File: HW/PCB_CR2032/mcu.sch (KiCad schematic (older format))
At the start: 15 parts, among them U1 STM32L071CBTx, Y1 32768 Hz

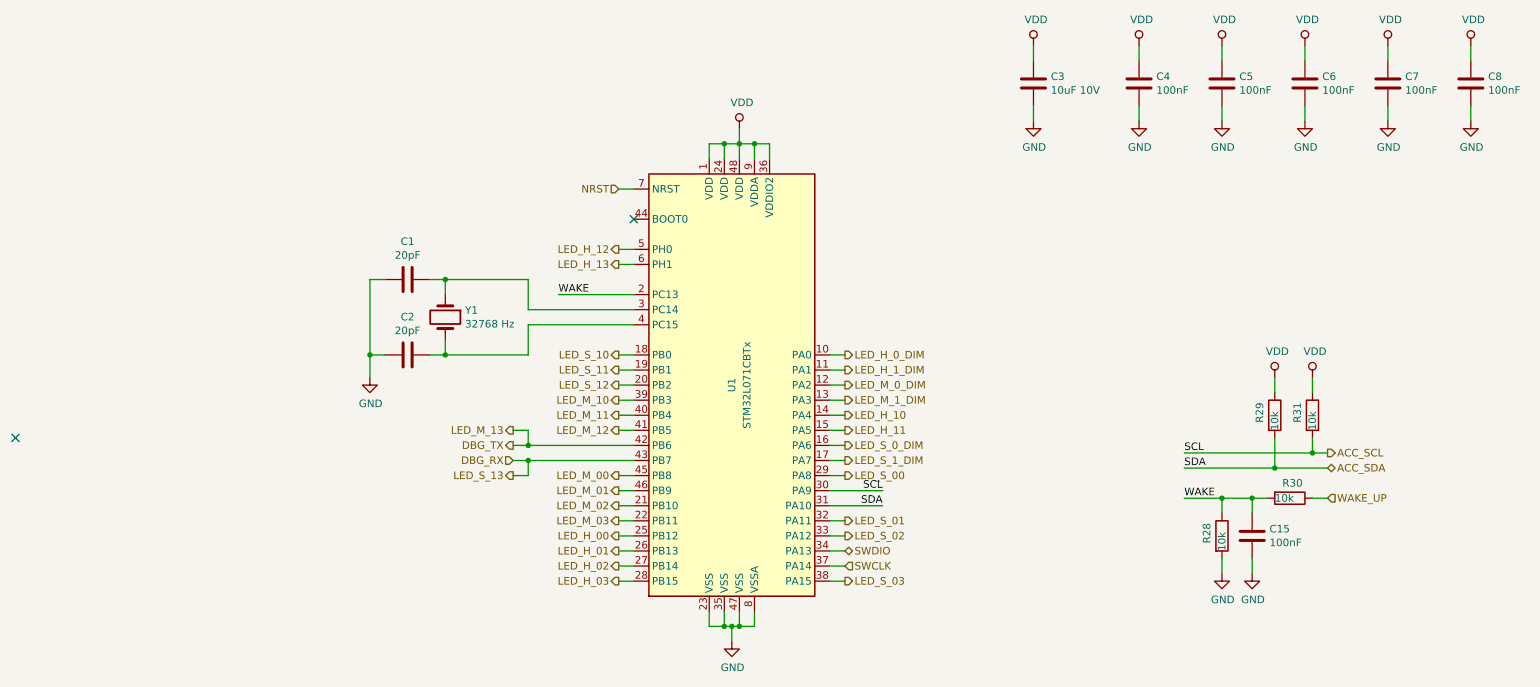
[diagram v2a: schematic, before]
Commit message: Created layout for CR2032 version 1.0, for first prototype order, resulted in a lot of changes in the pin-mapping to make routing easier.
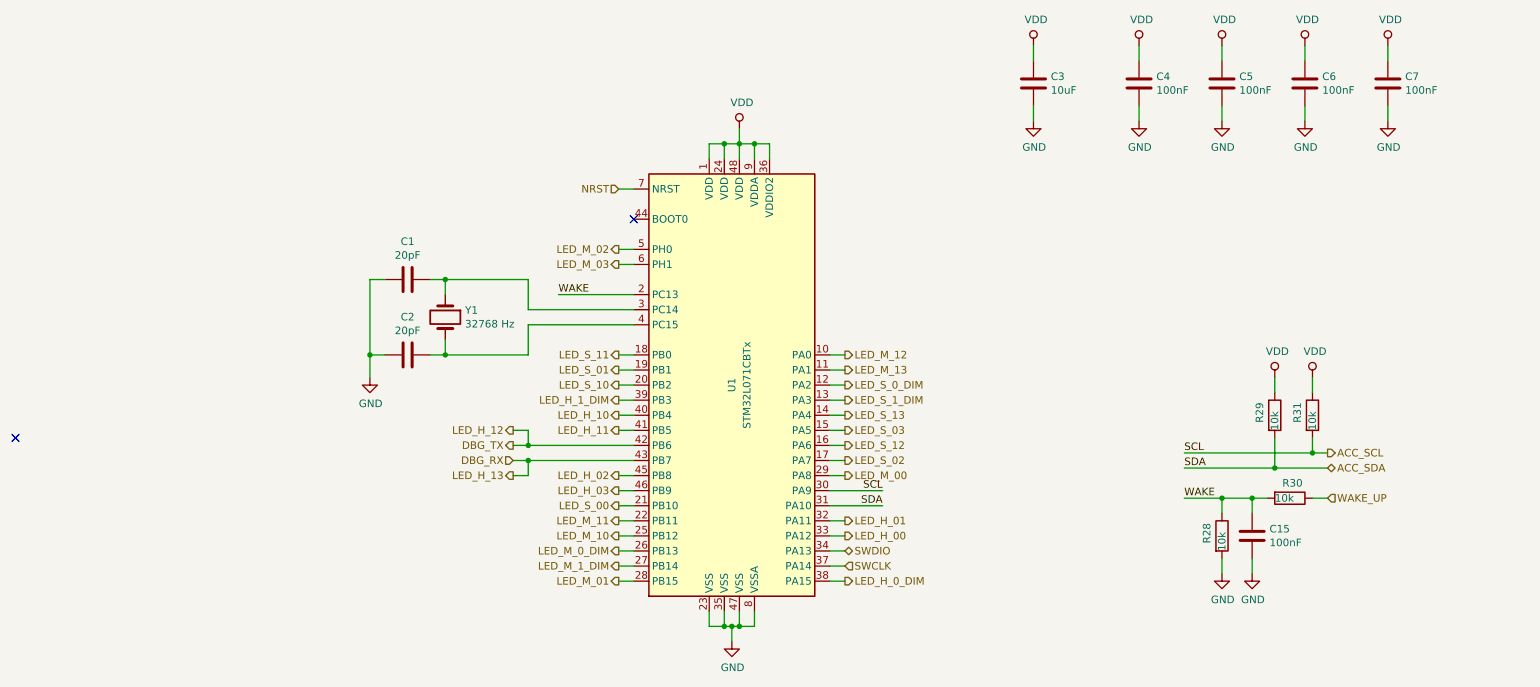
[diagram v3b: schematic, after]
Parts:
- removed C8: 100nF, Capacitor_SMD:C_0805_2012Metric_Pad1.15x1.40mm_HandSolder, symbol Device:C
- C1, C2: footprint Capacitor_SMD:C_0805_2012Metric_Pad1.15x1.40mm_HandSolder -> Capacitor_SMD:C_0603_1608Metric_Pad1.05x0.95mm_HandSolder; LCSC (none) -> C1648; Make Yageo -> (none); Mouser 603-CC805JRNPO9BN200 -> (none); Part CC0805JRNPO9BN200 -> (none); jlcpcb (none) -> CL10C200JB8NNNC
- C15, C4, C5, C6, C7: footprint Capacitor_SMD:C_0805_2012Metric_Pad1.15x1.40mm_HandSolder -> Capacitor_SMD:C_0603_1608Metric_Pad1.05x0.95mm_HandSolder; LCSC (none) -> C14663; Make Yageo -> (none); Mouser 603-CC805KRX7R9BB104 -> (none); Part CC0805KRX7R9BB104 -> (none); jlcpcb (none) -> CC0603KRX7R9BB104
- C3: value 10uF 10V -> 10uF; LCSC (none) -> C15850; Make Yageo -> (none); Mouser 603-CC805KKX7R6BB106 -> (none); Part CC0805KKX7R6BB106 -> (none); jlcpcb (none) -> CL21A106KAYNNNE
- R28, R29, R30, R31: footprint Resistor_SMD:R_0805_2012Metric_Pad1.15x1.40mm_HandSolder -> Resistor_SMD:R_0603_1608Metric_Pad1.05x0.95mm_HandSolder; LCSC (none) -> C25804; Make Yageo -> (none); Mouser 603-RC0805FR-0710KL -> (none); Part RC0805FR-0710KL -> (none); jlcpcb (none) -> 0603WAF1002T5E
- Y1: LCSC (none) -> C32346; jlcpcb (none) -> Q13FC1350000400
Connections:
- net LED_H_12 is gone; now on net LED_M_02: U1.5 (PH0)
- net LED_H_13 is gone; now on net LED_M_03: U1.6 (PH1)
- net LED_H_00: now also U1.33 (PA12); no longer U1.25 (PB12)
- net LED_H_01: now also U1.32 (PA11); no longer U1.26 (PB13)
- net LED_H_02: now also U1.45 (PB8); no longer U1.27 (PB14)
- net LED_H_03: now also U1.46 (PB9); no longer U1.28 (PB15)
- net LED_H_0_DIM: now also U1.38 (PA15); no longer U1.10 (PA0)
- net LED_H_10: now also U1.40 (PB4); no longer U1.14 (PA4)
- net LED_H_11: now also U1.41 (PB5); no longer U1.15 (PA5)
- net LED_H_1_DIM: now also U1.39 (PB3); no longer U1.11 (PA1)
- net LED_M_00: now also U1.29 (PA8); no longer U1.45 (PB8)
- net LED_M_01: now also U1.28 (PB15); no longer U1.46 (PB9)
- net LED_M_02: no longer U1.21 (PB10)
- net LED_M_03: no longer U1.22 (PB11)
- net LED_M_0_DIM: now also U1.26 (PB13); no longer U1.12 (PA2)
- net LED_M_10: now also U1.25 (PB12); no longer U1.39 (PB3)
- net LED_M_11: now also U1.22 (PB11); no longer U1.40 (PB4)
- net LED_M_12: now also U1.10 (PA0); no longer U1.41 (PB5)
- net LED_M_1_DIM: now also U1.27 (PB14); no longer U1.13 (PA3)
- net LED_S_00: now also U1.21 (PB10); no longer U1.29 (PA8)
- net LED_S_01: now also U1.19 (PB1); no longer U1.32 (PA11)
- net LED_S_02: now also U1.17 (PA7); no longer U1.33 (PA12)
- net LED_S_03: now also U1.15 (PA5); no longer U1.38 (PA15)
- net LED_S_0_DIM: now also U1.12 (PA2); no longer U1.16 (PA6)
- net LED_S_10: now also U1.20 (PB2); no longer U1.18 (PB0)
- net LED_S_11: now also U1.18 (PB0); no longer U1.19 (PB1)
- net LED_S_12: now also U1.16 (PA6); no longer U1.20 (PB2)
- net LED_S_1_DIM: now also U1.13 (PA3); no longer U1.17 (PA7)
- new net LED_M_13: U1.11 (PA1)
- new net LED_S_13: U1.14 (PA4)

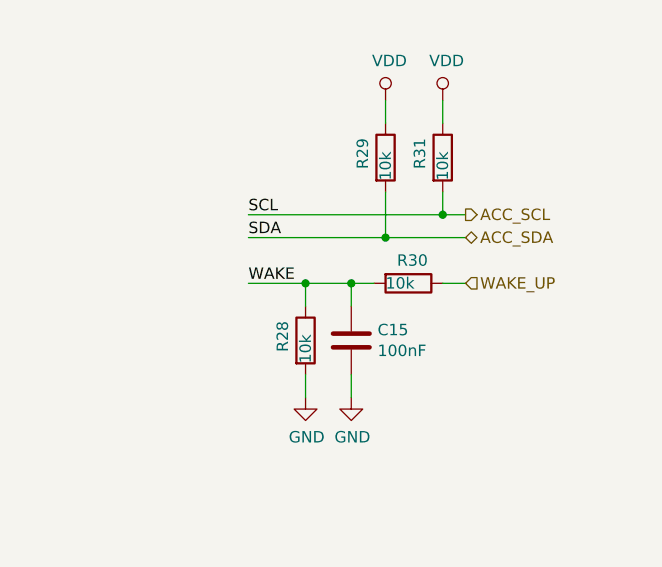
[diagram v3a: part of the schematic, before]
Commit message: Worked on Rev 2.0 HW with smaller size.
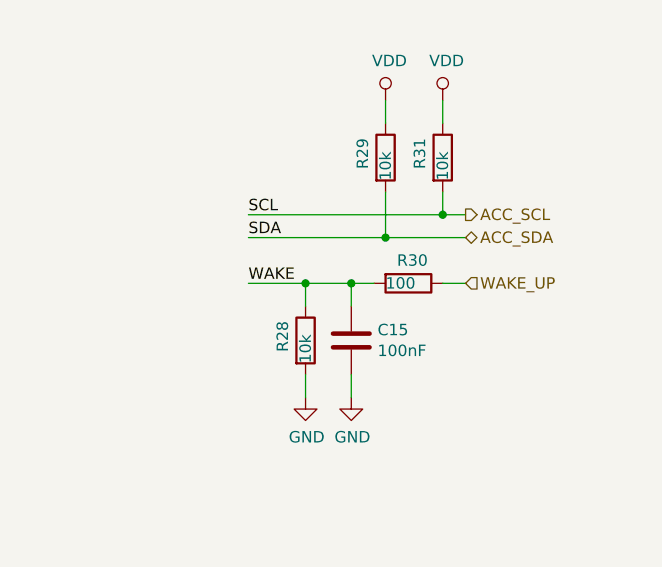
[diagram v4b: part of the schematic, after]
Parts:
- R30: value 10k -> 100
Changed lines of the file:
@@
 P 9200 4250
 F 0 "R30" V 9100 4200 50  0000 L CNN
-F 1 "10k" V 9200 4150 50  0000 L CNN
+F 1 "100" V 9200 4150 50  0000 L CNN
 F 2 "Resistor_SMD:R_0603_1608Metric_Pad1.05x0.95mm_HandSolder" V 9130 4250 50  0001 C CNN
 F 3 "~" H 9200 4250 50  0001 C CNN

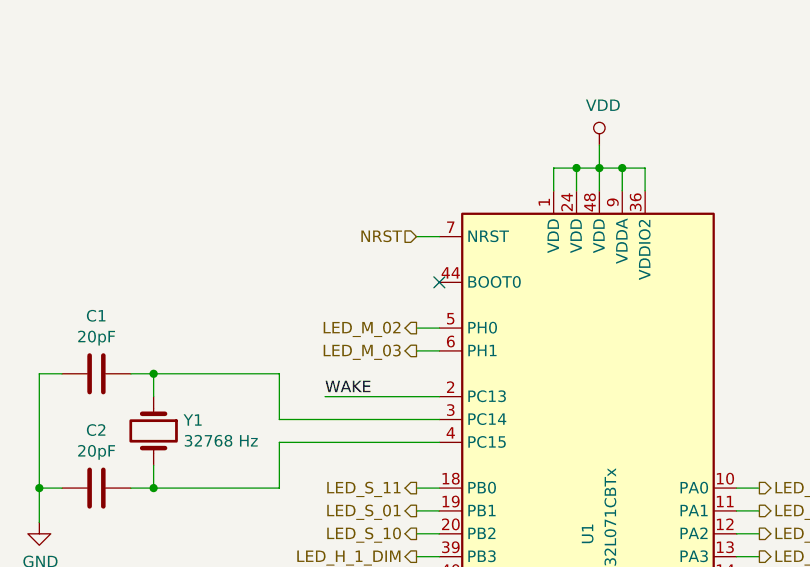
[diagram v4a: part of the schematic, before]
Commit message: Connected BOOT0 pin to GND after forst board bring up.
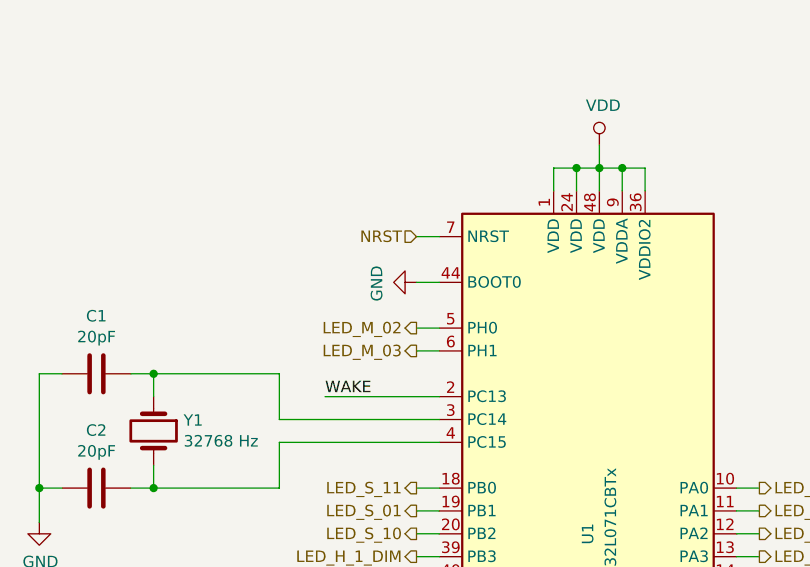
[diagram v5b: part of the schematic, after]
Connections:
- net GND: now also U1.44 (BOOT0)
- no-connect marks 2 -> 1
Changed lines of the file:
@@
 Wire Wire Line
 	9850 1350 9850 1250
-NoConn ~ 4850 2400
 Text HLabel 4750 3600 0    50   Output ~ 0
 LED_H_1_DIM
@@
 Wire Wire Line
 	4150 4000 4850 4000
+$Comp
+L power:GND #PWR0104
+U 1 1 5DD61BE4
+P 4750 2400
+F 0 "#PWR0104" H 4750 2150 50  0001 C CNN
+F 1 "GND" H 4755 2227 50  0000 C CNN
+F 2 "" H 4750 2400 50  0001 C CNN
+F 3 "" H 4750 2400 50  0001 C CNN
+	1    4750 2400
+	0    1    1    0
+$EndComp
+Wire Wire Line
+	4850 2400 4750 2400
 $EndSCHEMATC

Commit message: Ordered V2.0 PCB
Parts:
- R30: LCSC C25804 -> C22775
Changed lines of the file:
@@
 F 5 "" H 9200 4250 50  0001 C CNN "Mouser"
 F 6 "" H 9200 4250 50  0001 C CNN "Part"
-F 7 "C25804" H 9200 4250 50  0001 C CNN "LCSC"
+F 7 "C22775" H 9200 4250 50  0001 C CNN "LCSC"
 F 8 "0603WAF1002T5E" H 9200 4250 50  0001 C CNN "jlcpcb"
 	1    9200 4250
